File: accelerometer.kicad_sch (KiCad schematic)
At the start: 7 parts, among them U8 MPU-6050_C24112

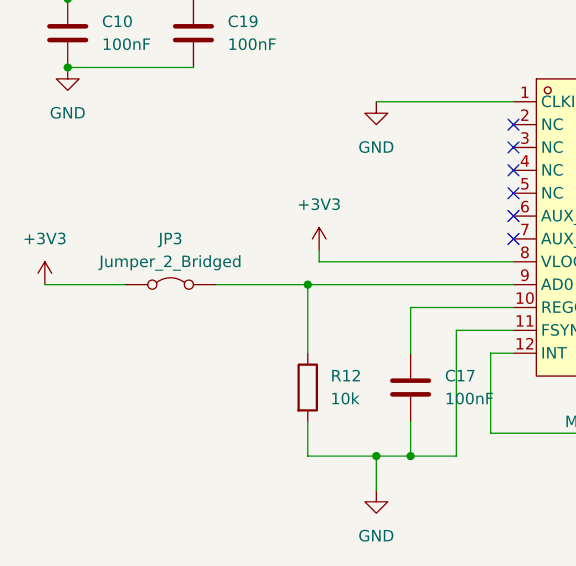
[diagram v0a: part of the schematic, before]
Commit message: Fixed fabrication files, so PCBA will work with the correct rotation of the components.
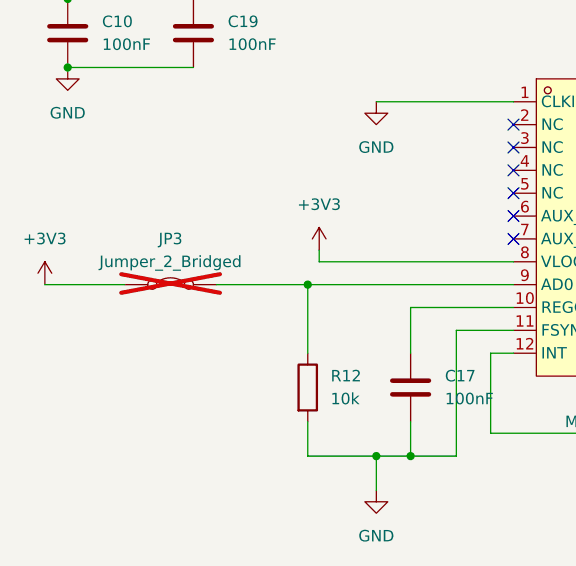
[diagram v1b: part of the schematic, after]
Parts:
- C10, C17, C19: LCSC C14663 -> C49678
- JP3: now not fitted; now left out of the parts list
- U8: Rotation Offset (none) -> 270
